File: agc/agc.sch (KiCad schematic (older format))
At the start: 66 parts, among them J5 SIL10, K1 SMD_HDR, K10 SMD_HDR, K11 SMD_HDR, K2 SMD_HDR, K3 SMD_HDR, K4 SMD_HDR, K5 SMD_HDR, K6 SMD_HDR, K7 SMD_HDR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

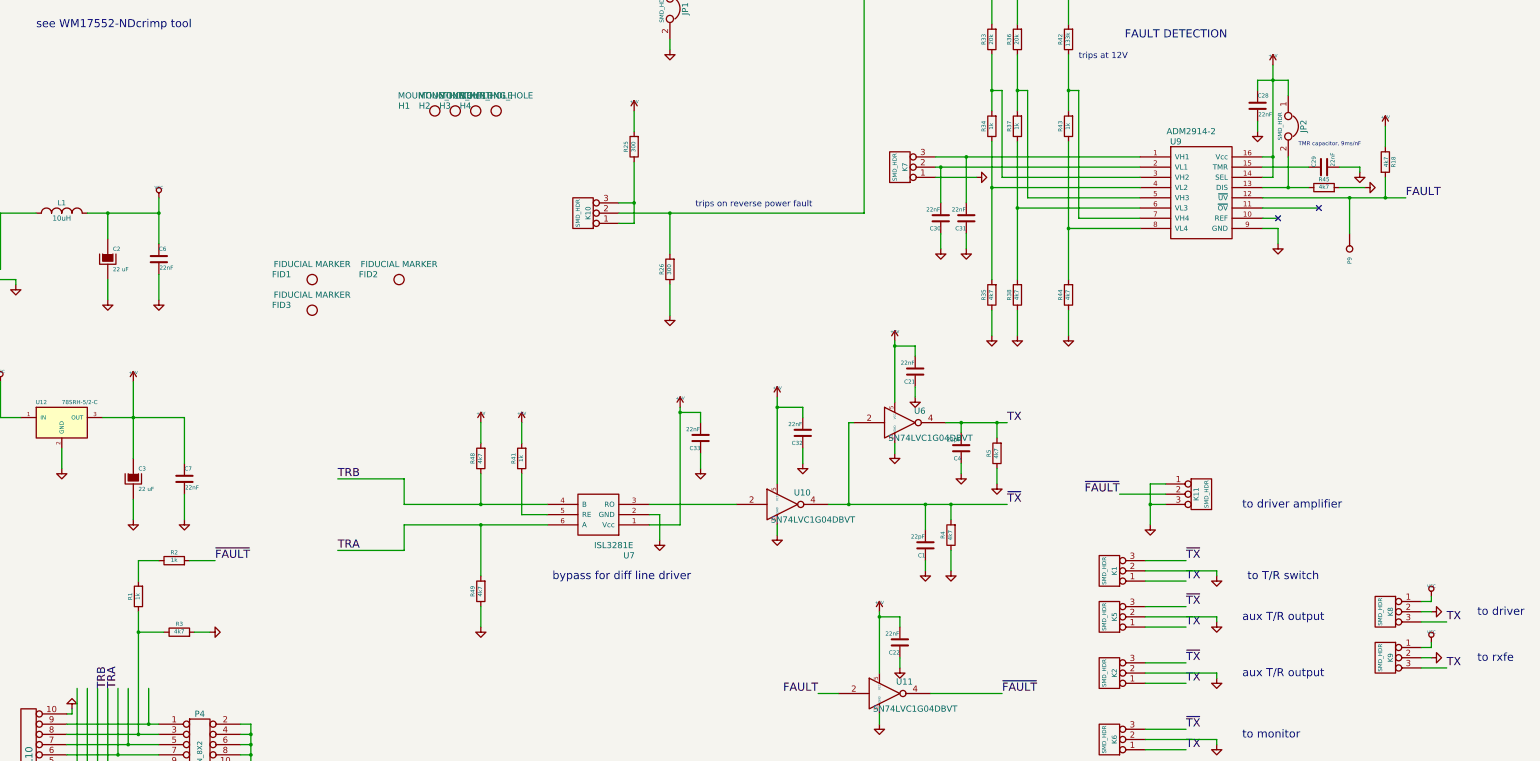
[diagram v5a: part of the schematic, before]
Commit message: added breakout board for usrp dio - allow cases to be closed during operation by routing all io through dio header
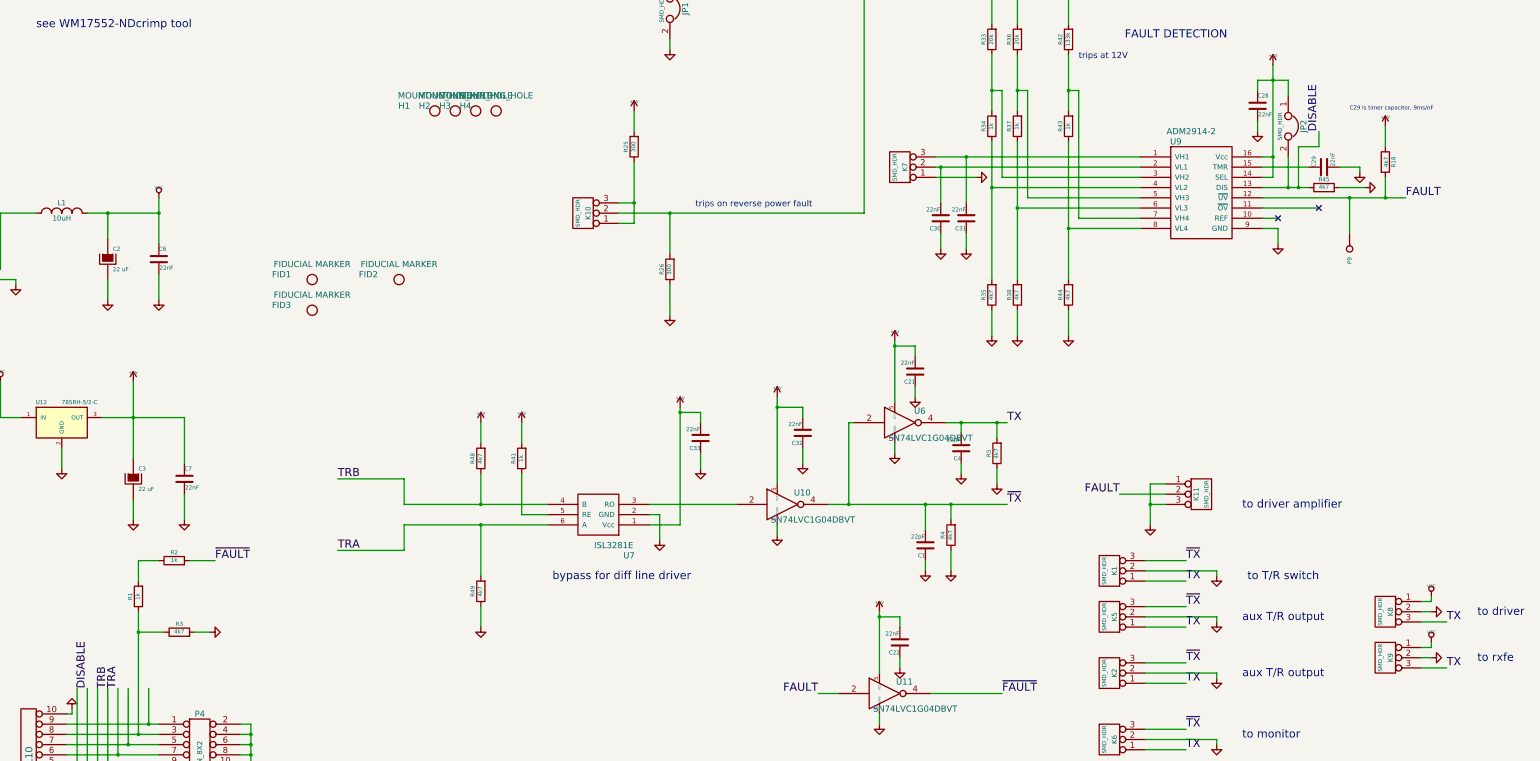
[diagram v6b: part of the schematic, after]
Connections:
- net FAULT: now also K11.2 (PM)
- net ~FAULT: no longer K11.2 (PM)
- net DISABLE: now reaches JP2.2, R45.1, U9.13 (DIS)
- net DISABLE: now also J5.3, P4.13
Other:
- note added: "C29 is timer capacitor, 9ms/nF\n"
- note removed: "TMR capacitor, 9ms/nF\n"
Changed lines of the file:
@@
 ~FAULT
 Text Label 12500 6650 2    79   ~ 0
-~FAULT
+FAULT
 $Comp
 L GND #PWR044
@@
 	1    0    0    -1
 $EndComp
-Text Notes 14250 3250 0    39   ~ 0
-TMR capacitor, 9ms/nF\n
+Text Notes 14750 2900 0    39   ~ 0
+C29 is timer capacitor, 9ms/nF\n
 Text Label 13150 8300 0    79   ~ 0
 ~TX
@@
 Text Notes 12100 2400 0    60   ~ 0
 trips at 12V
+Wire Wire Line
+	14250 3250 14250 3650
+Connection ~ 14250 3650
+Text Label 14450 3100 1    79   ~ 0
+DISABLE
+Wire Wire Line
+	14250 3250 14450 3250
+Wire Wire Line
+	14450 3250 14450 3100
+Text Label 2400 8550 1    79   ~ 0
+DISABLE
 $EndSCHEMATC

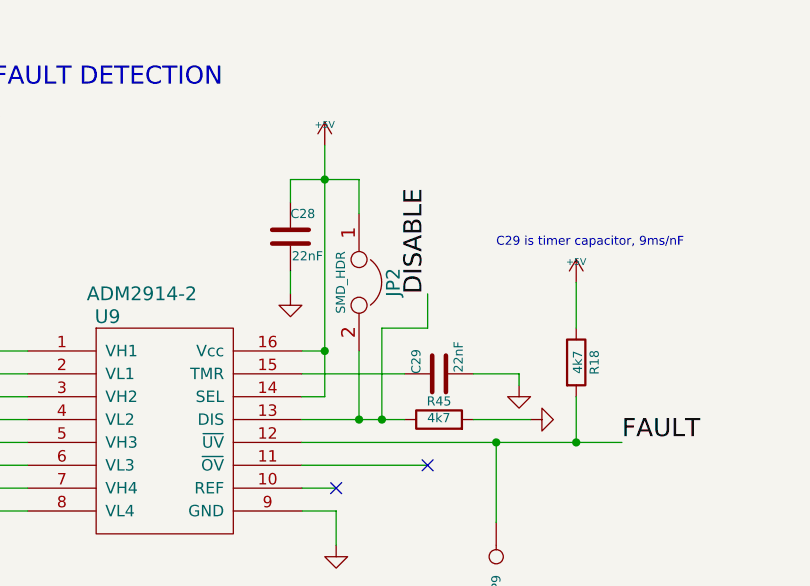
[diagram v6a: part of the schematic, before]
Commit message: modified hptr for higher power resistors
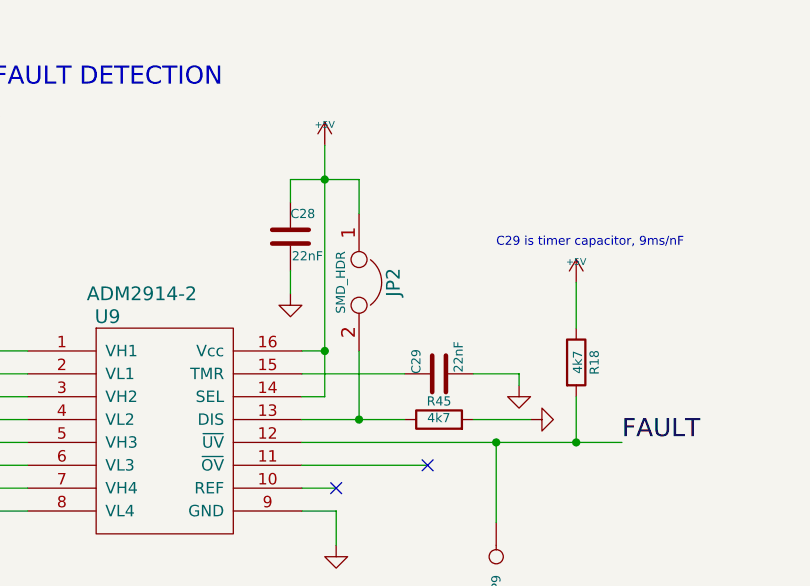
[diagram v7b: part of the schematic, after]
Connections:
- net DISABLE: no longer JP2.2, R45.1, U9.13 (DIS)
- new net: JP2.2, R45.1, U9.13 (DIS)
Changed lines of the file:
@@
 Text Notes 12100 2400 0    60   ~ 0
 trips at 12V
-Wire Wire Line
-	14250 3250 14250 3650
-Connection ~ 14250 3650
-Text Label 14450 3100 1    79   ~ 0
-DISABLE
-Wire Wire Line
-	14250 3250 14450 3250
-Wire Wire Line
-	14450 3250 14450 3100
 Text Label 2400 8550 1    79   ~ 0
 DISABLE

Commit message: committing modified files, I forget.., probably dfm
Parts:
- C1, C4, R18, R3, R4, R5: footprint SMD_Packages:SMD-0805 -> smd_capacitors:c_0805
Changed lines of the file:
@@
 F 0 "R18" V 15180 3400 40  0000 C CNN
 F 1 "4k7" V 15107 3401 40  0000 C CNN
-F 2 "SMD_Packages:SMD-0805" V 15030 3400 30  0001 C CNN
+F 2 "smd_capacitors:c_0805" V 15030 3400 30  0001 C CNN
 F 3 "" H 15100 3400 30  0000 C CNN
 F 4 "PANASONIC ELECTRONIC COMPONENTS (VA)" H 15100 3400 60  0001 C CNN "MFG Name"
@@
 F 0 "R3" V 3380 8000 40  0000 C CNN
 F 1 "4k7" V 3307 8001 40  0000 C CNN
-F 2 "SMD_Packages:SMD-0805" V 3230 8000 30  0001 C CNN
+F 2 "smd_capacitors:c_0805" V 3230 8000 30  0001 C CNN
 F 3 "" H 3300 8000 30  0000 C CNN
 F 4 "PANASONIC ELECTRONIC COMPONENTS (VA)" H 3300 8000 60  0001 C CNN "MFG Name"
@@
 F 0 "C1" H 10600 7250 40  0000 L CNN
 F 1 "22pF" H 10606 7065 40  0000 L CNN
-F 2 "SMD_Packages:SMD-0805" H 10638 7000 30  0001 C CNN
+F 2 "smd_capacitors:c_0805" H 10638 7000 30  0001 C CNN
 F 3 "" H 10600 7150 60  0000 C CNN
 F 4 "SAMSUNG ELECTRO-MECHANICS AMERICA, INC (VA)" H 10600 7150 60  0001 C CNN "MFG Name"
@@
 F 0 "C4" H 10950 6300 40  0000 L CNN
 F 1 "22pF" H 10956 6115 40  0000 L CNN
-F 2 "SMD_Packages:SMD-0805" H 10988 6050 30  0001 C CNN
+F 2 "smd_capacitors:c_0805" H 10988 6050 30  0001 C CNN
 F 3 "" H 10950 6200 60  0000 C CNN
 F 4 "SAMSUNG ELECTRO-MECHANICS AMERICA, INC (VA)" H 10950 6200 60  0001 C CNN "MFG Name"
@@
 F 0 "R5" V 11380 6250 40  0000 C CNN
 F 1 "4k7" V 11307 6251 40  0000 C CNN
-F 2 "SMD_Packages:SMD-0805" V 11230 6250 30  0001 C CNN
+F 2 "smd_capacitors:c_0805" V 11230 6250 30  0001 C CNN
 F 3 "" H 11300 6250 30  0000 C CNN
 F 4 "PANASONIC ELECTRONIC COMPONENTS (VA)" H 11300 6250 60  0001 C CNN "MFG Name"
@@
 F 0 "R4" V 10930 7050 40  0000 C CNN
 F 1 "4k7" V 10857 7051 40  0000 C CNN
-F 2 "SMD_Packages:SMD-0805" V 10780 7050 30  0001 C CNN
+F 2 "smd_capacitors:c_0805" V 10780 7050 30  0001 C CNN
 F 3 "" H 10850 7050 30  0000 C CNN
 F 4 "PANASONIC ELECTRONIC COMPONENTS (VA)" H 10850 7050 60  0001 C CNN "MFG Name"
